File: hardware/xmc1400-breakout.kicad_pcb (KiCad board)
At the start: 2 copper layers, 50 x 45 mm, 34 parts, among them P1 CON-SENSOR2, P2 BOOT, P3 CONN_01X12, P4 CONN_01X12, P5 CONN_01X12, P6 CONN_01X12, P7 CONN_02X04, U1 XMC1XXX48, U2 DRILL, U3 DRILL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

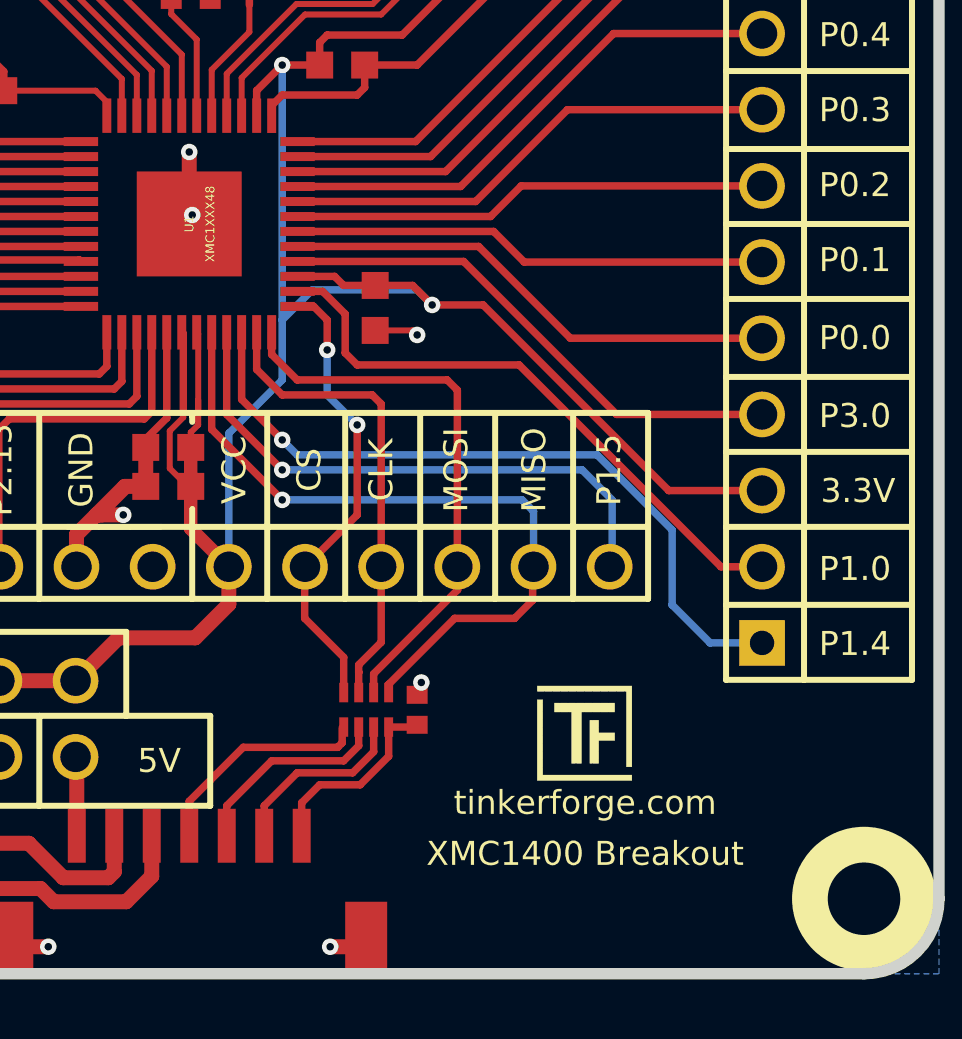
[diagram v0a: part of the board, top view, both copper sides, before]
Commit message: fix file names
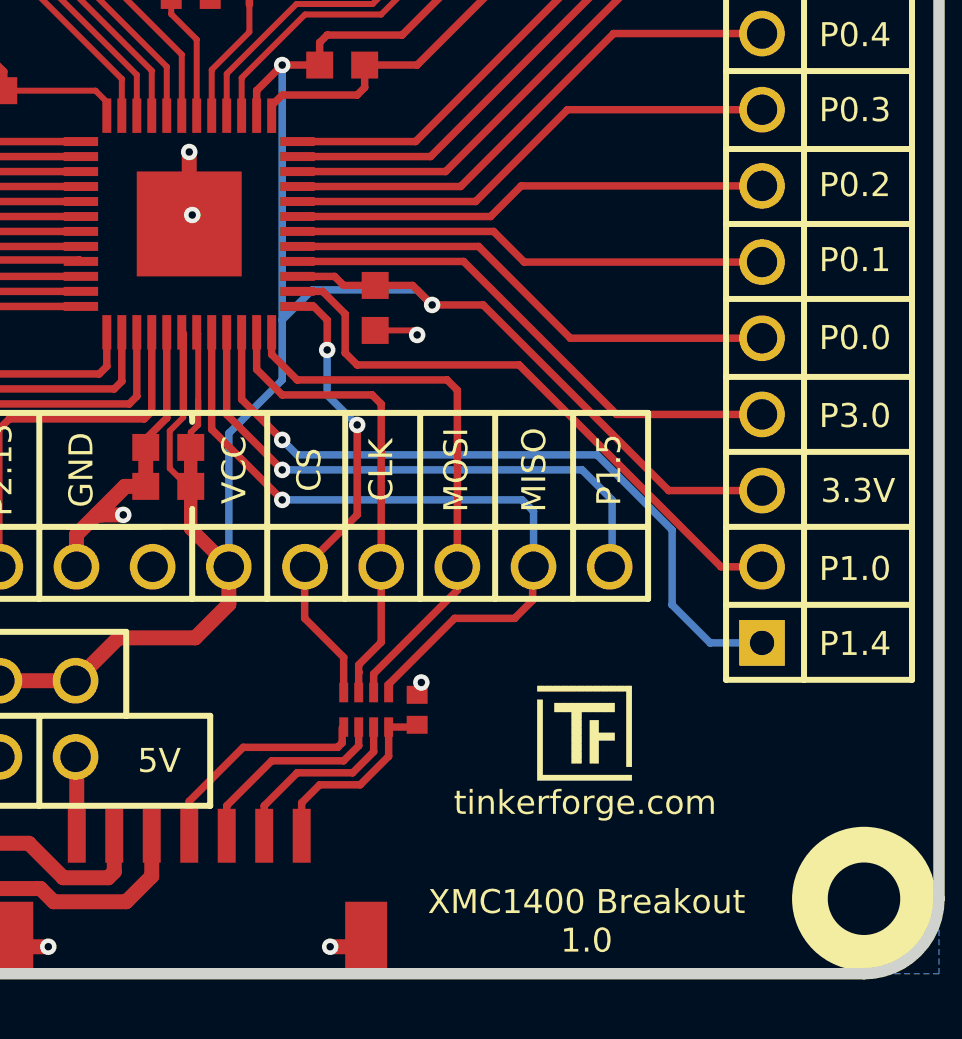
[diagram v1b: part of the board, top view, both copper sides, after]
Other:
- board text added: "XMC1400 Breakout 1.0"
- board text removed: "XMC1400 Breakout"

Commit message: specify processor
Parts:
- U1: value XMC1XXX48 -> XMC1404
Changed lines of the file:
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@@
       (effects (font (size 0.29972 0.29972) (thickness 0.0762)))
     )
-    (fp_text value XMC1XXX48 (at 0 -0.7 270) (layer F.Fab)
-      (effects (font (size 0.29972 0.29972) (thickness 0.0762)))
+    (fp_text value XMC1404 (at 0 -0.7 270) (layer F.Fab)
+      (effects (font (size 0.29972 0.29972) (thickness 0.07493)))
     )
     (fp_line (start -3.49758 3.49758) (end -3.49758 3.49758) (layer F.SilkS) (width 0.00254))

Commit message: specify resistor
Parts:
- R9: value TBD -> DNP
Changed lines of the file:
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@@
       (effects (font (size 0.2 0.2) (thickness 0.05)))
     )
-    (fp_text value TBD (at 0 -0.275) (layer F.Fab)
+    (fp_text value DNP (at 0 -0.275) (layer F.Fab)
       (effects (font (size 0.2 0.2) (thickness 0.05)))
     )
